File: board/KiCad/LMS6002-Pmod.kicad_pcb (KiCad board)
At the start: 2 copper layers, 76.2 x 48.8 mm, 58 parts, among them CON1 BARREL_JACK, J1 FX10B_80S_8, J2 Pinheader_1x6_TH, J3 SELECT_DIV, P1 PMOD_2x6, P2 PMOD_2x6, P3 Myriad_Mount_Hole, P4 Myriad_Mount_Hole, Q1 Q_PMOS_GSD, SW1 ICE_RESET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

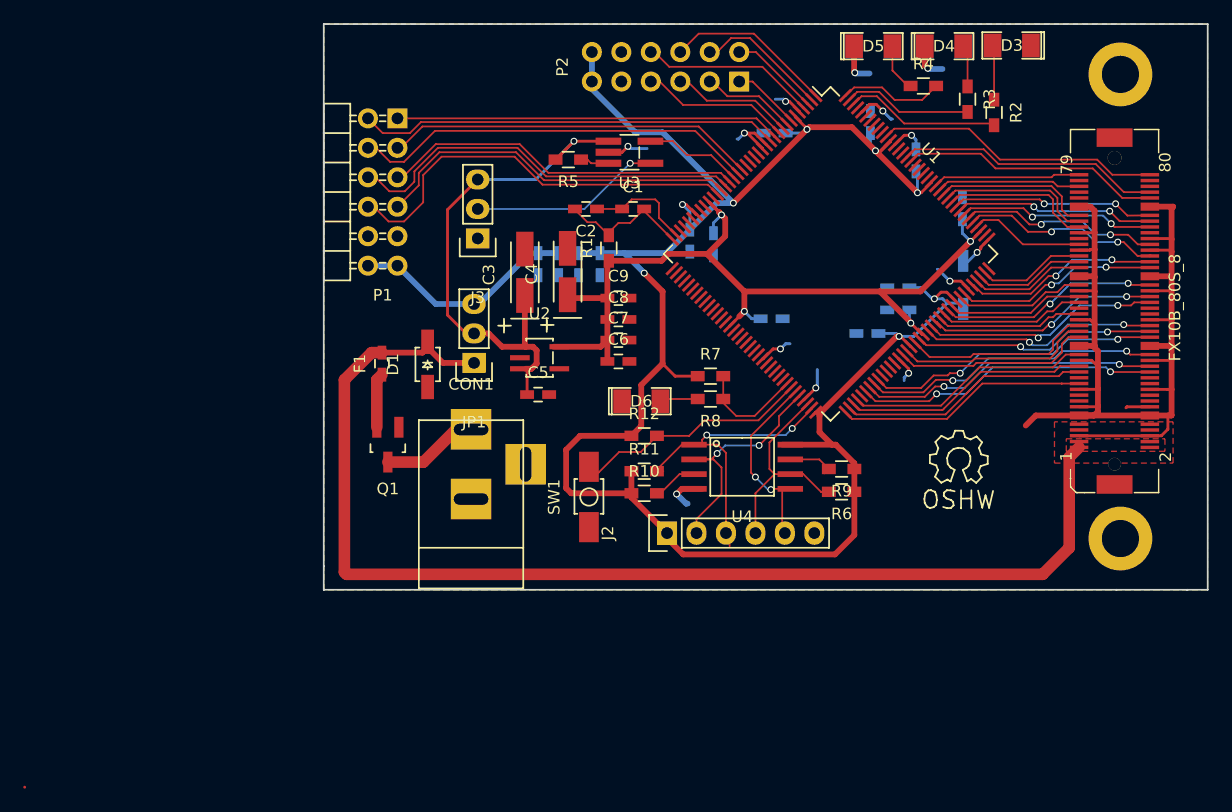
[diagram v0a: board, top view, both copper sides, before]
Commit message: Fix silkscreen
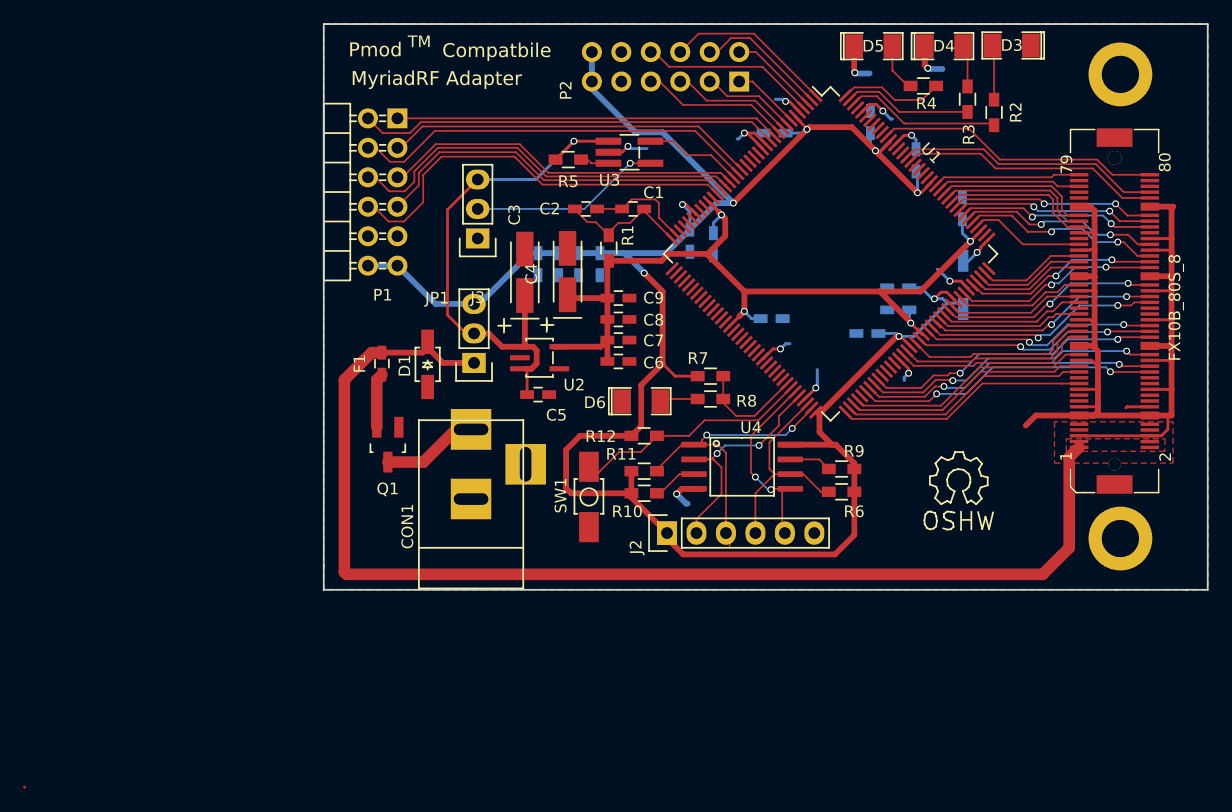
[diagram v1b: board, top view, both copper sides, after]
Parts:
- moved T1 1.84 mm to (153.8, 105.4)
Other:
- board text added: "Compatbile"
- board text added: "MyriadRF Adapter"
- board text added: "Pmod"
- board text added: "TM"
